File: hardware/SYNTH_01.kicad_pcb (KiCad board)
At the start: 2 copper layers, 112.7 x 150 mm, 55 parts, among them J2 Conn_01x04_Pin, SW1 SW_Push_45deg, SW10 SW_Push_45deg, SW11 SW_Push_45deg, SW12 SW_Push_45deg, SW13 SW_Push_45deg, SW14 SW_Push_45deg, SW15 SW_Push_45deg, SW16 SW_Push_45deg, SW17 SW_Push_45deg, SW18 SW_Push_45deg, SW19 SW_Push_45deg, SW2 SW_Push_45deg, SW20 SW_Push_45deg, SW21 SW_Push_45deg, SW3 SW_Push_45deg, SW4 SW_Push_45deg, SW5 SW_Push_45deg, SW6 SW_Push_45deg, SW7 SW_Push_45deg, SW8 SW_Push_45deg, SW9 SW_Push_45deg, U1 MCP23017-E/SP

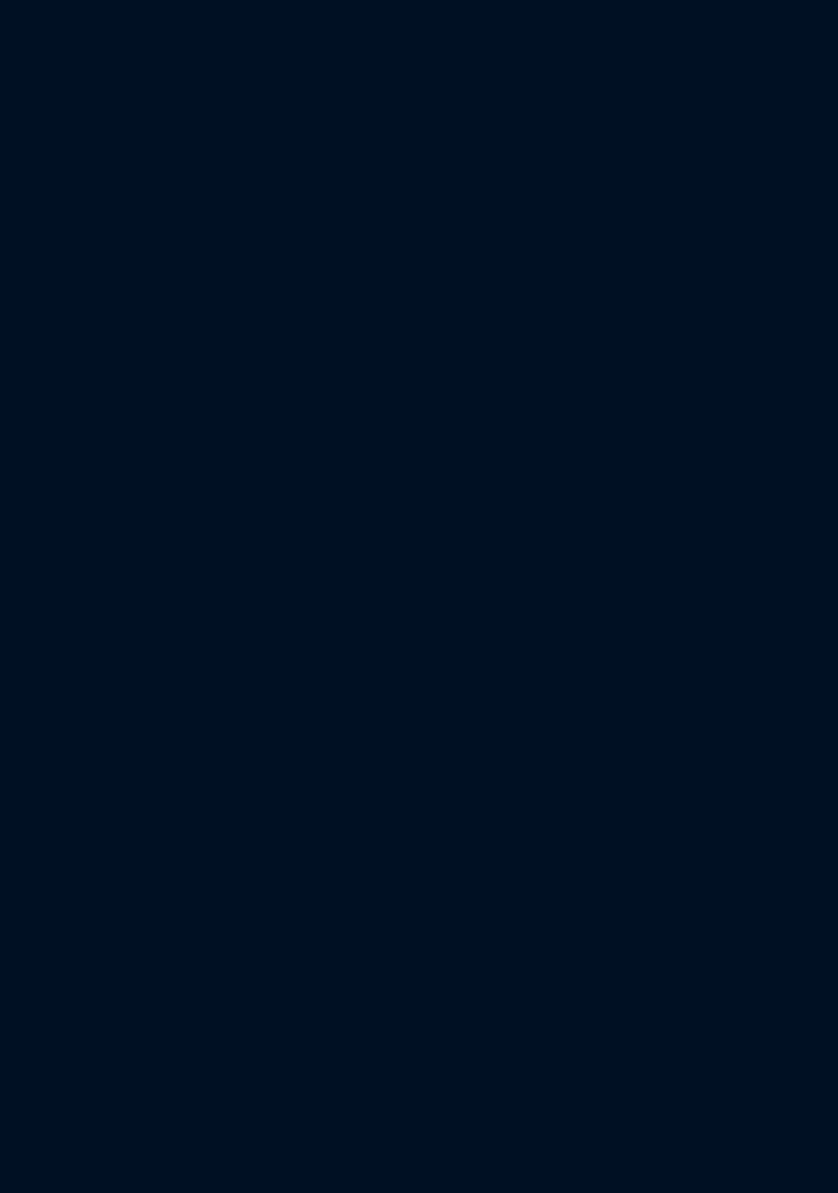
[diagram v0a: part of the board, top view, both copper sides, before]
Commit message: PCB: updating PCB with new RGB sch
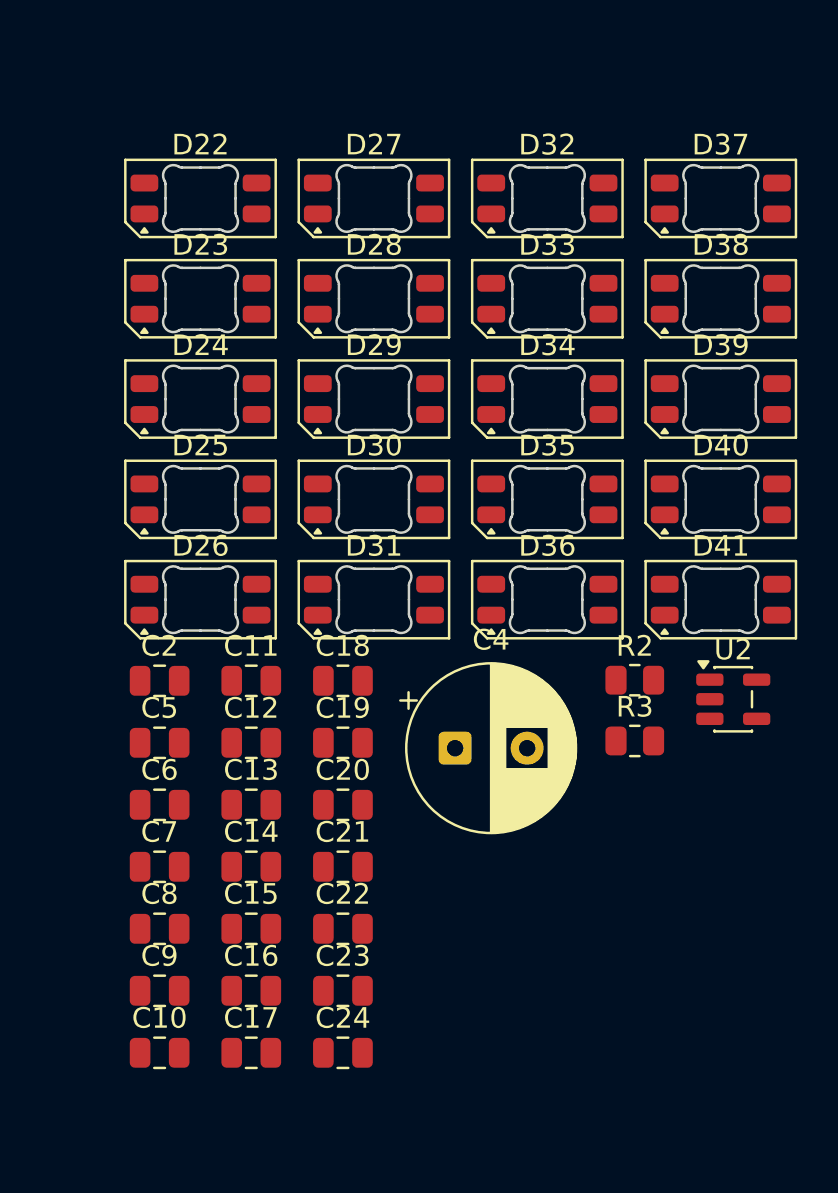
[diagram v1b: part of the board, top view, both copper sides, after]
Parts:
- added C10: 100nF, Capacitor_SMD:C_0805_2012Metric, F.Cu at (185.1, 79.1)
- added C11: 100nF, Capacitor_SMD:C_0805_2012Metric, F.Cu at (189.5, 61.1)
- added C12: 100nF, Capacitor_SMD:C_0805_2012Metric, F.Cu at (189.5, 64.1)
- added C13: 100nF, Capacitor_SMD:C_0805_2012Metric, F.Cu at (189.5, 67.1)
- added C14: 100nF, Capacitor_SMD:C_0805_2012Metric, F.Cu at (189.5, 70.1)
- added C15: 100nF, Capacitor_SMD:C_0805_2012Metric, F.Cu at (189.5, 73.1)
- added C16: 100nF, Capacitor_SMD:C_0805_2012Metric, F.Cu at (189.5, 76.1)
- added C17: 100nF, Capacitor_SMD:C_0805_2012Metric, F.Cu at (189.5, 79.1)
- added C18: 100nF, Capacitor_SMD:C_0805_2012Metric, F.Cu at (194.0, 61.1)
- added C19: 100nF, Capacitor_SMD:C_0805_2012Metric, F.Cu at (194.0, 64.1)
- added C2: 100nF, Capacitor_SMD:C_0805_2012Metric, F.Cu at (185.1, 61.1)
- added C20: 100nF, Capacitor_SMD:C_0805_2012Metric, F.Cu at (194.0, 67.1)
- added C21: 100nF, Capacitor_SMD:C_0805_2012Metric, F.Cu at (194.0, 70.1)
- added C22: 100nF, Capacitor_SMD:C_0805_2012Metric, F.Cu at (194.0, 73.1)
- added C23: 100nF, Capacitor_SMD:C_0805_2012Metric, F.Cu at (194.0, 76.1)
- added C24: 100nF, Capacitor_SMD:C_0805_2012Metric, F.Cu at (194.0, 79.1)
- added C4: 470 µF / 10 V, Capacitor_THT:CP_Radial_D8.0mm_P3.50mm, F.Cu at (199.4, 64.3)
- added C5: 100nF, Capacitor_SMD:C_0805_2012Metric, F.Cu at (185.1, 64.1)
- added C6: 100nF, Capacitor_SMD:C_0805_2012Metric, F.Cu at (185.1, 67.1)
- added C7: 100nF, Capacitor_SMD:C_0805_2012Metric, F.Cu at (185.1, 70.1)
- added C8: 100nF, Capacitor_SMD:C_0805_2012Metric, F.Cu at (185.1, 73.1)
- added C9: 100nF, Capacitor_SMD:C_0805_2012Metric, F.Cu at (185.1, 76.1)
- added D22: SK6812MINI-E, LED_SMD:LED_SK6812MINI-E_3.2x2.8mm_P1.5mm_ReverseMount, F.Cu at (187.1, 37.7)
- added D23: SK6812MINI-E, LED_SMD:LED_SK6812MINI-E_3.2x2.8mm_P1.5mm_ReverseMount, F.Cu at (187.1, 42.5)
- added D24: SK6812MINI-E, LED_SMD:LED_SK6812MINI-E_3.2x2.8mm_P1.5mm_ReverseMount, F.Cu at (187.1, 47.4)
- added D25: SK6812MINI-E, LED_SMD:LED_SK6812MINI-E_3.2x2.8mm_P1.5mm_ReverseMount, F.Cu at (187.1, 52.3)
- added D26: SK6812MINI-E, LED_SMD:LED_SK6812MINI-E_3.2x2.8mm_P1.5mm_ReverseMount, F.Cu at (187.1, 57.1)
- added D27: SK6812MINI-E, LED_SMD:LED_SK6812MINI-E_3.2x2.8mm_P1.5mm_ReverseMount, F.Cu at (195.5, 37.7)
- added D28: SK6812MINI-E, LED_SMD:LED_SK6812MINI-E_3.2x2.8mm_P1.5mm_ReverseMount, F.Cu at (195.5, 42.5)
- added D29: SK6812MINI-E, LED_SMD:LED_SK6812MINI-E_3.2x2.8mm_P1.5mm_ReverseMount, F.Cu at (195.5, 47.4)
- added D30: SK6812MINI-E, LED_SMD:LED_SK6812MINI-E_3.2x2.8mm_P1.5mm_ReverseMount, F.Cu at (195.5, 52.3)
- added D31: SK6812MINI-E, LED_SMD:LED_SK6812MINI-E_3.2x2.8mm_P1.5mm_ReverseMount, F.Cu at (195.5, 57.1)
- added D32: SK6812MINI-E, LED_SMD:LED_SK6812MINI-E_3.2x2.8mm_P1.5mm_ReverseMount, F.Cu at (203.9, 37.7)
- added D33: SK6812MINI-E, LED_SMD:LED_SK6812MINI-E_3.2x2.8mm_P1.5mm_ReverseMount, F.Cu at (203.9, 42.5)
- added D34: SK6812MINI-E, LED_SMD:LED_SK6812MINI-E_3.2x2.8mm_P1.5mm_ReverseMount, F.Cu at (203.9, 47.4)
- added D35: SK6812MINI-E, LED_SMD:LED_SK6812MINI-E_3.2x2.8mm_P1.5mm_ReverseMount, F.Cu at (203.9, 52.3)
- added D36: SK6812MINI-E, LED_SMD:LED_SK6812MINI-E_3.2x2.8mm_P1.5mm_ReverseMount, F.Cu at (203.9, 57.1)
- added D37: SK6812MINI-E, LED_SMD:LED_SK6812MINI-E_3.2x2.8mm_P1.5mm_ReverseMount, F.Cu at (212.3, 37.7)
- added D38: SK6812MINI-E, LED_SMD:LED_SK6812MINI-E_3.2x2.8mm_P1.5mm_ReverseMount, F.Cu at (212.3, 42.5)
- added D39: SK6812MINI-E, LED_SMD:LED_SK6812MINI-E_3.2x2.8mm_P1.5mm_ReverseMount, F.Cu at (212.3, 47.4)
- added D40: SK6812MINI-E, LED_SMD:LED_SK6812MINI-E_3.2x2.8mm_P1.5mm_ReverseMount, F.Cu at (212.3, 52.3)
- added D41: SK6812MINI-E, LED_SMD:LED_SK6812MINI-E_3.2x2.8mm_P1.5mm_ReverseMount, F.Cu at (212.3, 57.1)
- added R2: 470, Resistor_SMD:R_0805_2012Metric, F.Cu at (208.2, 61.0)
- added R3: 10k, Resistor_SMD:R_0805_2012Metric, F.Cu at (208.2, 64.0)
- added U2: 74AHCT1G125, Package_TO_SOT_SMD:SOT-23-5, F.Cu at (212.9, 62.0)
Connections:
- net /COL0 renamed /SYNTH_01/COL0
- net /COL1 renamed /SYNTH_01/COL1
- net /COL2 renamed /SYNTH_01/COL2
- net /COL3 renamed /SYNTH_01/COL3
- net /COL_SHIFT renamed /SYNTH_01/COL_SHIFT
- net /E1_A renamed /SYNTH_01/E1_A
- net /E1_B renamed /SYNTH_01/E1_B
- net /E1_SW renamed /SYNTH_01/E1_SW
- net /E2_A renamed /SYNTH_01/E2_A
- net /E2_B renamed /SYNTH_01/E2_B
- net /E2_SW renamed /SYNTH_01/E2_SW
- net /E3_A renamed /SYNTH_01/E3_A
- net /E3_B renamed /SYNTH_01/E3_B
- net /E3_SW renamed /SYNTH_01/E3_SW
- net /E4_A renamed /SYNTH_01/E4_A
- net /E4_B renamed /SYNTH_01/E4_B
- net /E4_SW renamed /SYNTH_01/E4_SW
- net /E5_A renamed /SYNTH_01/E5_A
- net /E5_B renamed /SYNTH_01/E5_B
- net /E5_SW renamed /SYNTH_01/E5_SW
- net /E6_A renamed /SYNTH_01/E6_A
- net /E6_B renamed /SYNTH_01/E6_B
- net /E6_SW renamed /SYNTH_01/E6_SW
- net /E7_A renamed /SYNTH_01/E7_A
- net /E7_B renamed /SYNTH_01/E7_B
- net /E7_SW renamed /SYNTH_01/E7_SW
- net /ROW0 renamed /SYNTH_01/ROW0
- net /ROW1 renamed /SYNTH_01/ROW1
- net /ROW2 renamed /SYNTH_01/ROW2
- net /ROW3 renamed /SYNTH_01/ROW3
- net /ROW4 renamed /SYNTH_01/ROW4
- net /SCL renamed /SYNTH_01/SCL
- net /SDA renamed /SYNTH_01/SDA
- A1 pad 22: unconnected-(A1-GPIO17-Pad22) -> LED_DATA
- A1 pad 40: unconnected-(A1-VBUS-Pad40) -> LED_5V

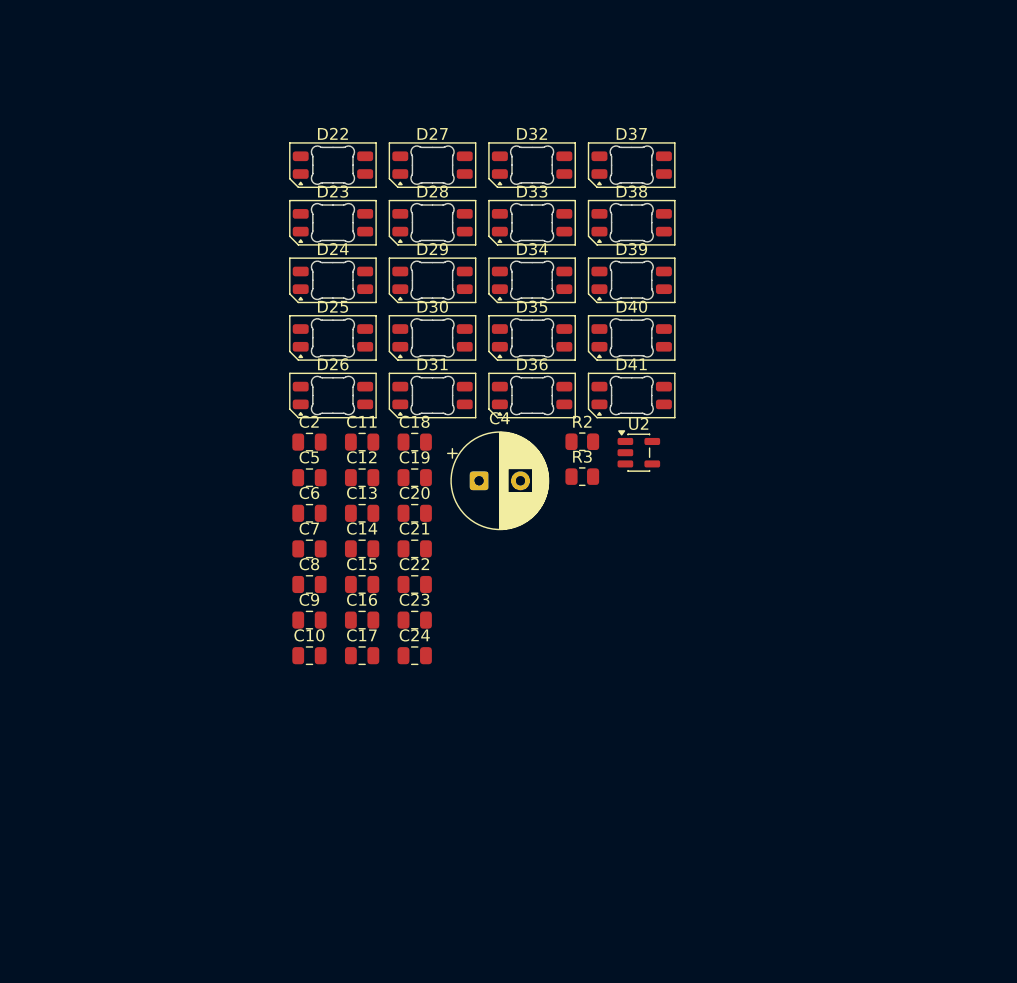
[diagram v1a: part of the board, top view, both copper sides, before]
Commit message: PCB: finished LEDs upgrade of the current PCB
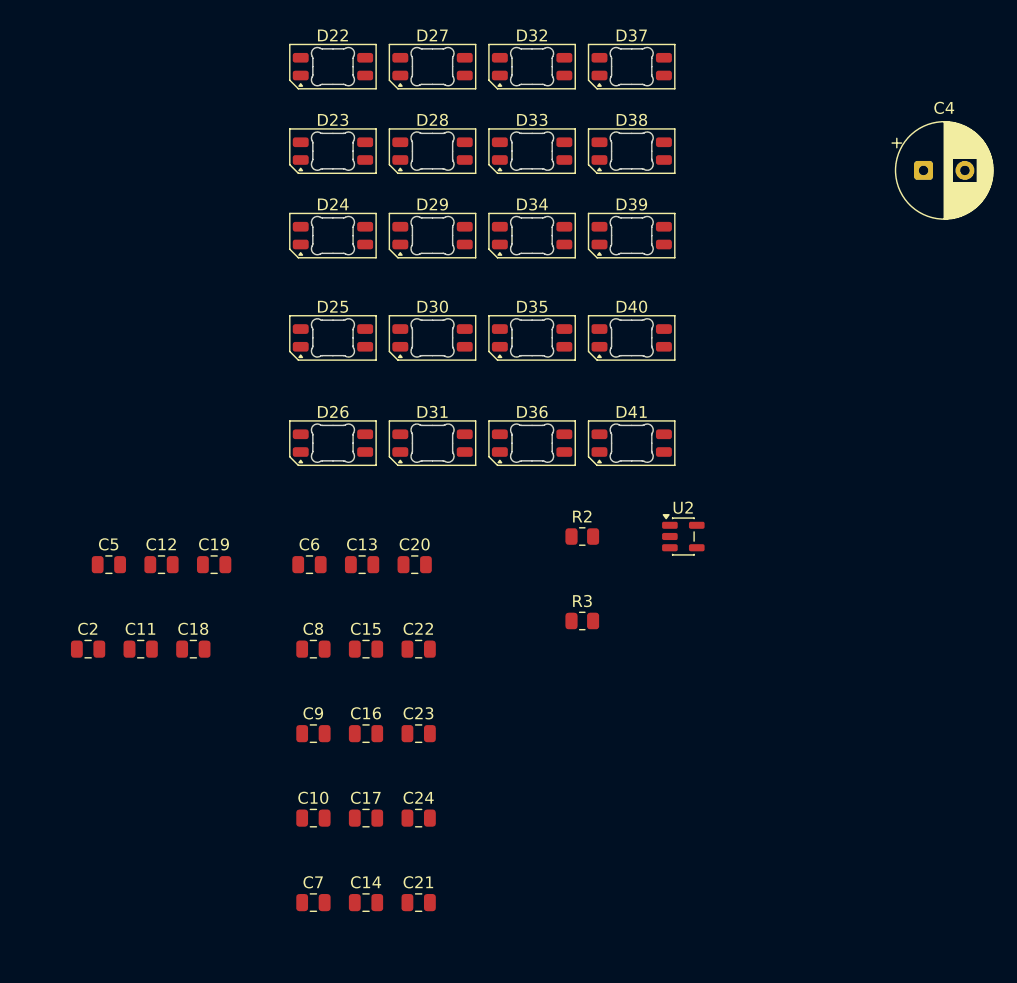
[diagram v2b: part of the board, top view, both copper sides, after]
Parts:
- moved C4 45.8 mm to (237.0, 38.1)
- moved C14 29.9 mm to (189.9, 100.0)
- moved C21 29.9 mm to (194.3, 100.0)
- moved C7 29.9 mm to (185.4, 100.0)
- moved C11 25.6 mm to (170.8, 78.6)
- moved C18 25.6 mm to (175.3, 78.6)
- moved C2 25.6 mm to (166.4, 78.6)
- moved C12 18.5 mm to (172.6, 71.4)
- moved C5 18.5 mm to (168.1, 71.4)
- moved C19 18.5 mm to (177.0, 71.4)
- moved C10 13.7 mm to (185.4, 92.9)
- moved C17 13.7 mm to (189.9, 92.9)
- moved C24 13.7 mm to (194.3, 92.9)
- moved R3 12.2 mm to (208.2, 76.2)
- moved C16 9.61 mm to (189.9, 85.7)
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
